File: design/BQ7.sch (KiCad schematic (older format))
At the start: 0 parts

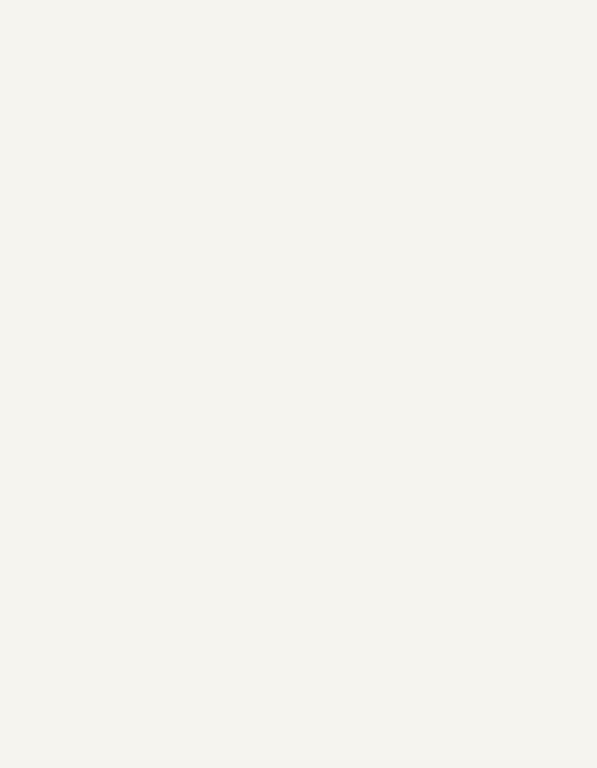
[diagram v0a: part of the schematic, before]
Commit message: Add new component bq and other libs also fix lib path. Project is now portable
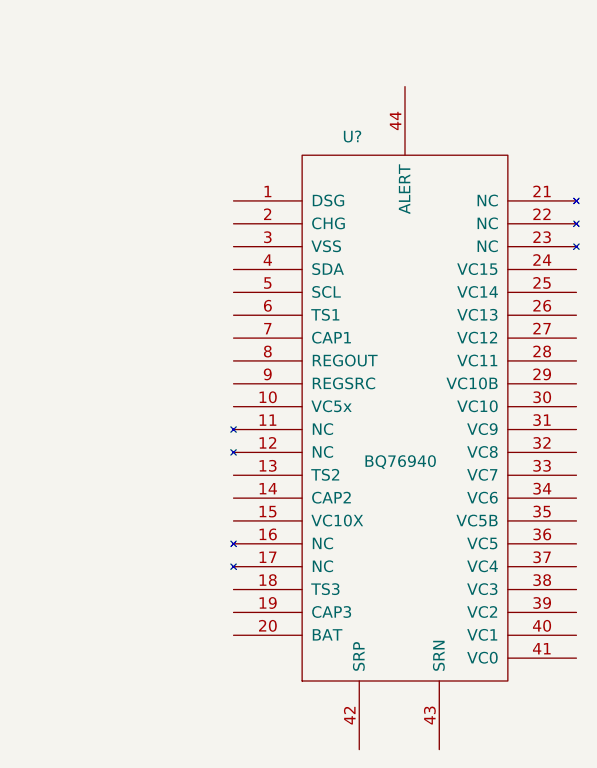
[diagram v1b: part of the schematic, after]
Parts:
- added U?: BQ76940, MODULE, symbol BQ76940
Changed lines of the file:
@@
 EESchema Schematic File Version 2
+LIBS:iso5500
+LIBS:crf_1
+LIBS:BQ76940
 LIBS:power
 LIBS:device
@@
 LIBS:contrib
 LIBS:valves
+LIBS:BMS-cache
 EELAYER 25 0
 EELAYER END
@@
 Text Notes 1150 1050 0    60   ~ 0
 Bq7*** circuit its basicly disconnetced from other stuff looking a\n voltage of every cell and if needed discharging them.(balancing)\nControled by a MCU two of them because we have 30 batterys.
+$Comp
+L BQ76940 U?
+U 1 1 55BBBEDC
+P 8550 2500
+F 0 "U?" H 8320 3730 50  0000 C CNN
+F 1 "BQ76940" H 8530 2310 50  0000 C CNN
+F 2 "MODULE" H 8590 3300 50  0001 C CNN
+F 3 "DOCUMENTATION" H 8500 930 50  0001 C CNN
+	1    8550 2500
+	1    0    0    -1
+$EndComp
 $EndSCHEMATC

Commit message: Some modification and started job
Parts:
- removed U?: BQ76940, MODULE, symbol BQ76940
- added C? (x3): 0.1u, symbol C
- added C?: 4.7u, symbol C
- added C? (x4): Cf, symbol C
- added C? (x2): C, symbol C
- added D? (x3): DIODE, symbol DIODE
- added D? (x2): DIODESCH, symbol DIODESCH
- added Q?: MOSFET_N, symbol MOSFET_N
- added R?: 1M, symbol R
- added R? (x3): 50k, symbol R
- added R?: SHUNT, symbol SHUNT
- added R? (x2): 100, symbol R
- added R?: Rgate, symbol R
- added R?: Rdrain, symbol R
- added R?: Rf 1M, symbol R
- added R?: Rd, symbol R
- added R?: Rsrc, symbol R
- added U?: BQ76940, MODULE, symbol BQ76940
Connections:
- new net: R?.1, U?.44 (ALERT)
- new net: R?.2, R?.3
- new net: R?.2, R?.4
- new net: C?.1, C?.1, R?.1, U?.43 (SRN)
- new net: C?.1, C?.2, R?.1
- new net: C?.1, U?.7 (CAP1)
- new net: C?.2, R?.2, U?.9 (REGSRC)
- new net: D?.2 (K), Q?.G, R?.1
- new net: D?.2 (K), Q?.D, R?.1
- new net: D?.1 (A), D?.1 (A), D?.2 (K), Q?.S, R?.1
- new net: D?.1 (A), D?.1 (A)
- new net: D?.2 (K), R?.1, R?.2
- new net +BATT: R?.2, R?.2
- new net -BATT: R?.1
- new net BATT: C?.1, C?.2, D?.2 (K), R?.1, U?.20 (BAT)
- new net GND: C?.1, C?.1, C?.2, C?.2, C?.2, C?.2, R?.1, R?.1, R?.1, R?.2, R?.2, U?.3 (VSS)
- new net NTC Temp monitor/Temp1_in: R?.2, U?.6 (TS1)
- new net NTC Temp monitor/Temp2_in: R?.2, U?.13 (TS2)
- new net NTC Temp monitor/Temp3_in: R?.2, U?.18 (TS3)
- new net SCL: U?.5 (SCL)
- new net SDA: U?.4 (SDA)
- new net VC10X: C?.1, C?.2, C?.2, R?.2, U?.15 (VC10X)
- new net VC15: D?.1 (A)
- new net VC5X: C?.1, C?.2, U?.10 (VC5x)
- new net Vcc: C?.1, U?.8 (REGOUT)
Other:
- note added: "Capactior between termistors"
- note added: "Dont forget this when programming"
- note added: "Max BAT-VSS = 36V/25V\nso R must be quite high \n1M"
- note added: "Pin configuration\n"
- note added: "Should be high value\n"

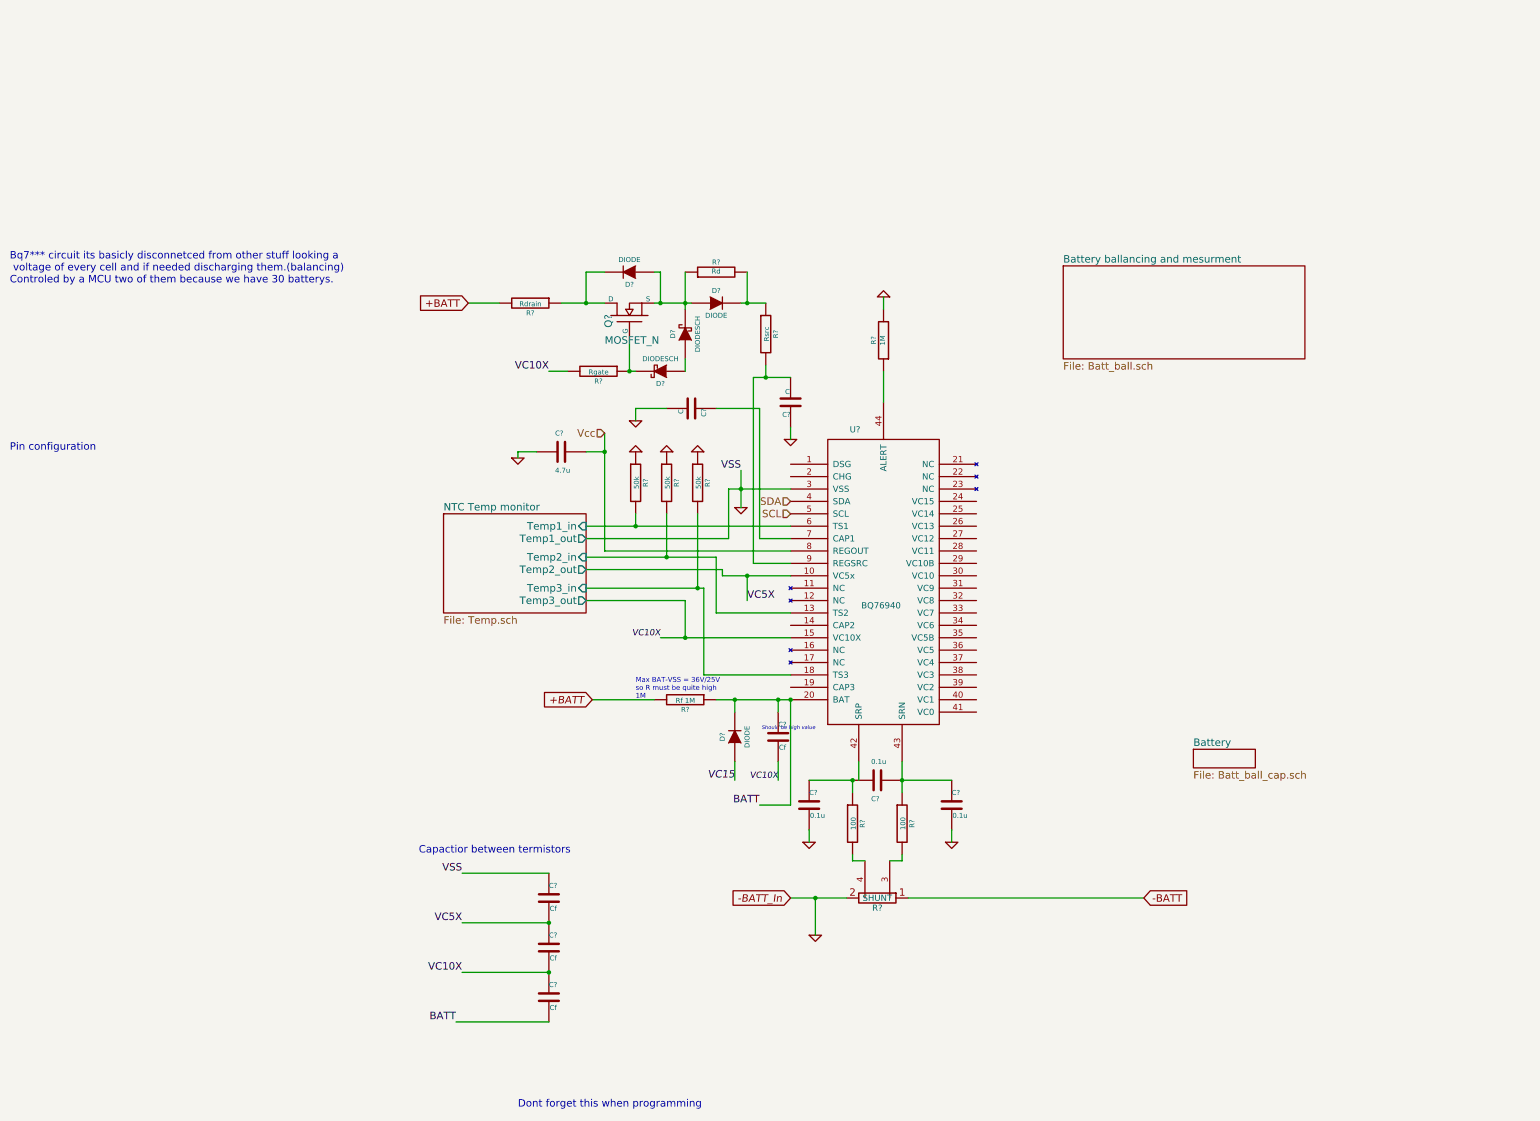
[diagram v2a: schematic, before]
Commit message: Add a cell to 10 but currently a scheme is a total mess fix it
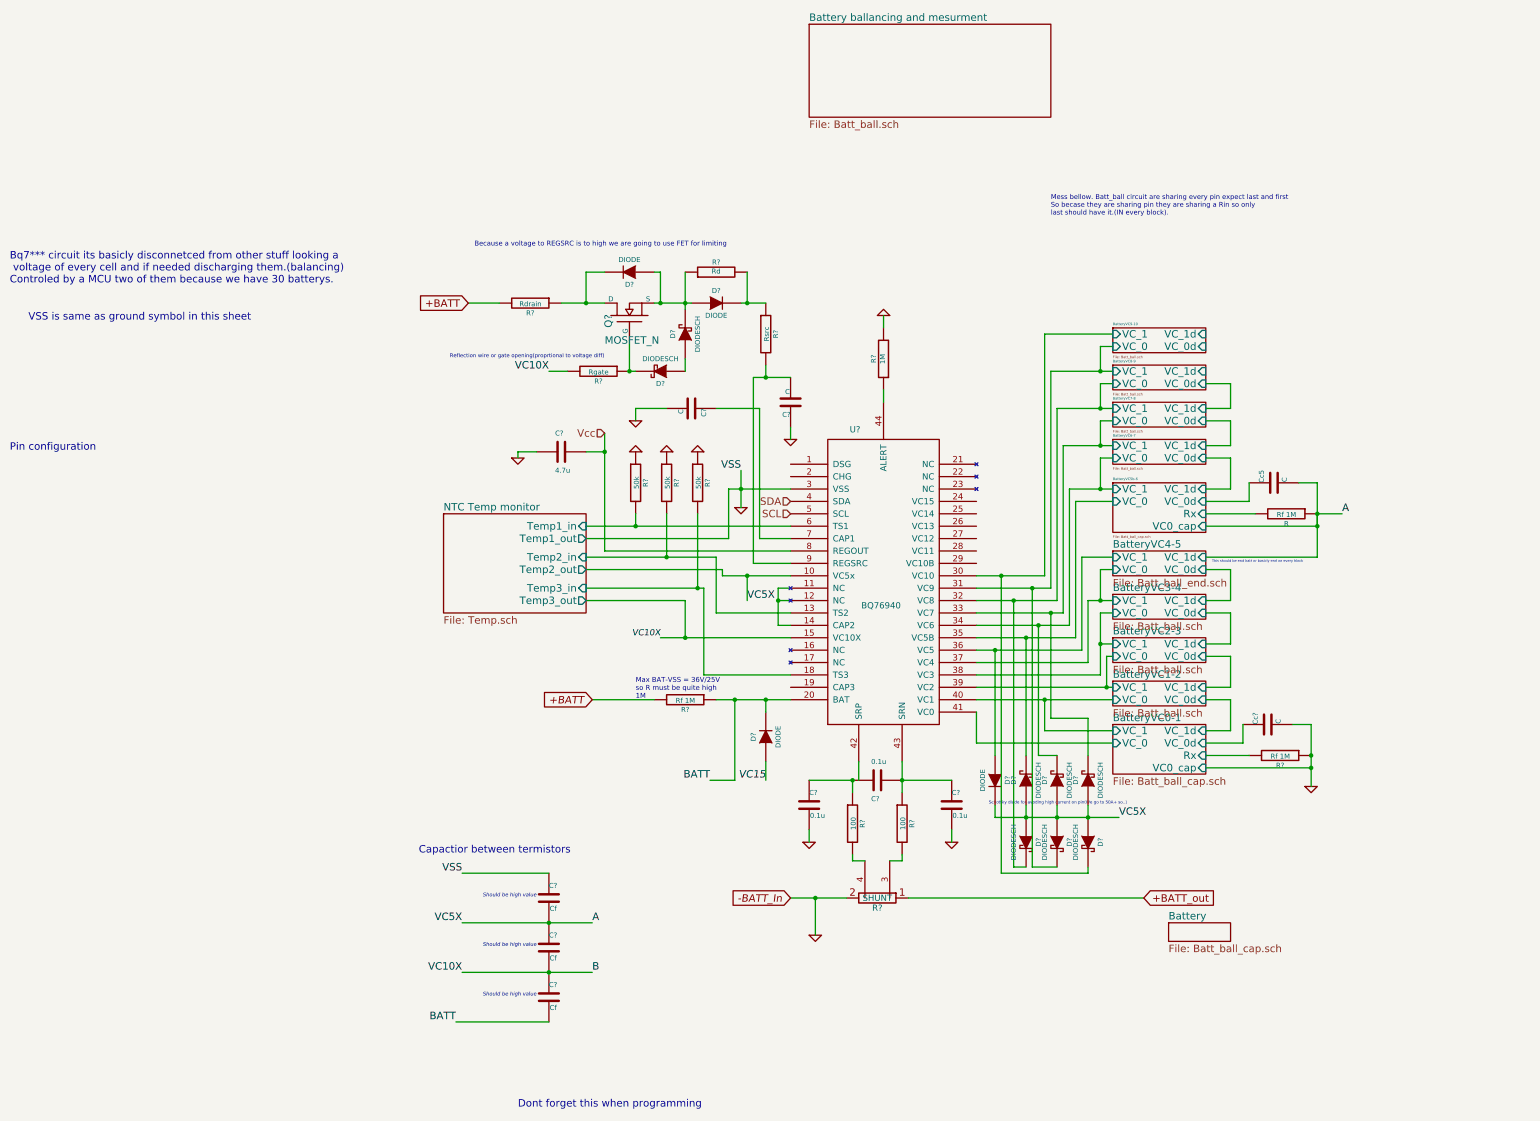
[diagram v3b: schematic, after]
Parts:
- removed C?: Cf, symbol C
- added Cc5, Cc?: C, symbol C
- added D?: DIODE, symbol DIODE
- added D? (x6): DIODESCH, symbol DIODESCH
- added R, R?: Rf 1M, symbol R
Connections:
- net GND: now also Cc?.2, R?.1
- net at U?.11 (NC): now also U?.12 (NC), U?.14 (CAP2)
- net BatteryVC9-10/VC_1: now reaches U?.30 (VC10)
- net BatteryVC9-10/VC_1: now also D?.2 (K)
- net BatteryVC8-9/VC_1: now reaches U?.31 (VC9)
- net BatteryVC8-9/VC_1: now also D?.2 (K)
- net BatteryVC7-8/VC_1: now reaches U?.32 (VC8)
- net BatteryVC7-8/VC_1: now also D?.2 (K)
- net BatteryVC6-7/VC_1: now reaches U?.33 (VC7)
- net BatteryVC6-7/VC_1: now also D?.2 (K)
- net BatteryVC5b-6/VC_1: now reaches U?.34 (VC6)
- net BatteryVC5b-6/VC_1: now also D?.2 (K)
- net BatteryVC5b-6/VC_0: now reaches U?.35 (VC5B)
- net BatteryVC5b-6/VC_0: now also D?.2 (K)
- net BatteryVC4-5/VC_1: now reaches U?.36 (VC5)
- net BatteryVC4-5/VC_1: now also D?.1 (A)
- net BatteryVC3-4/VC_1: now reaches U?.37 (VC4)
- net BatteryVC2-3/VC_1: now reaches U?.38 (VC3)
- net BatteryVC1-2/VC_1: now reaches U?.39 (VC2)
- net BatteryVC0-1/VC_1: now reaches U?.40 (VC1)
- net BatteryVC0-1/VC_0: now reaches U?.41 (VC0)
- net -BATT renamed +BATT_out
- net VC10X renamed B
- net VC5X renamed A
- net A: now also Cc5.2, D?.1 (A), D?.1 (A), D?.1 (A), D?.1 (A), D?.1 (A), D?.1 (A), D?.2 (K), R.1
- new net BatteryVC0-1/Rx: R?.2
- new net BatteryVC0-1/VC_0d: Cc?.1
- new net BatteryVC5b-6/Rx: R.2
- new net BatteryVC5b-6/VC_0d: Cc5.1
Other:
- note added: "Because a voltage to REGSRC is to high we are going to use FET for limiting"
- note added: "Mess bellow. Batt_ball circuit are sharing every pin expect last and first\nSo becase they are sharing pin they are sharing a Rin so only\nlast should have it.(IN every block)."
- note added: "Reflection wire or gate opening(proprtional to voltage diff)"
- note added: "Schottky diode for avoding high current on pin(We go to 50A+ so..)"
- note added: "This should be end batt or basicly end on every block"
- note added: "VSS is same as ground symbol in this sheet"
- moved on the sheet: D?, R?

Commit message: Fix BQ scheme so it's more readable
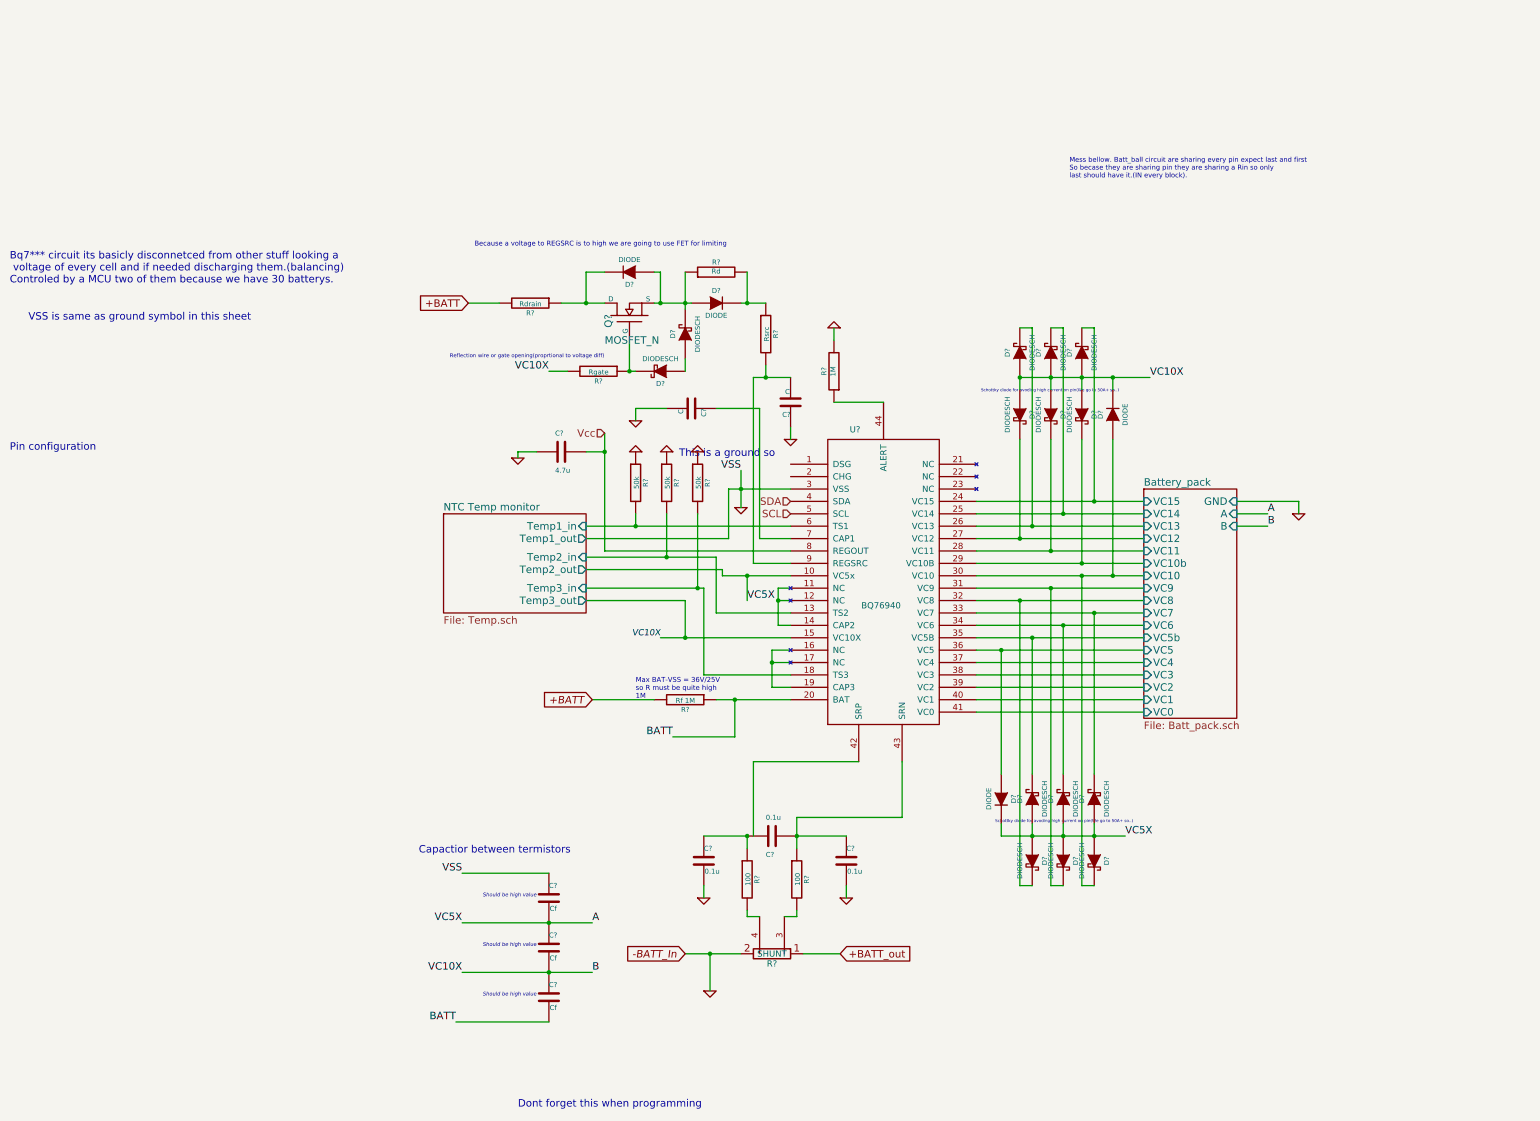
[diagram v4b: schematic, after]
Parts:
- removed Cc5, Cc?: C, symbol C
- removed D?: DIODE, symbol DIODE
- removed R, R?: Rf 1M, symbol R
- added D?: DIODE, symbol DIODE
- added D? (x6): DIODESCH, symbol DIODESCH
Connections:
- net B: now also D?.1 (A), D?.1 (A), D?.1 (A), D?.1 (A), D?.1 (A), D?.1 (A), D?.2 (K)
- net at U?.16 (NC): now also U?.17 (NC), U?.19 (CAP3)
- net Battery_pack/VC15: now reaches U?.24 (VC15)
- net Battery_pack/VC15: now also D?.2 (K)
- net Battery_pack/VC14: now reaches U?.25 (VC14)
- net Battery_pack/VC14: now also D?.2 (K)
- net Battery_pack/VC13: now reaches U?.26 (VC13)
- net Battery_pack/VC13: now also D?.2 (K)
- net Battery_pack/VC12: now reaches U?.27 (VC12)
- net Battery_pack/VC12: now also D?.2 (K)
- net Battery_pack/VC11: now reaches U?.28 (VC11)
- net Battery_pack/VC11: now also D?.2 (K)
- net Battery_pack/VC10b: now reaches U?.29 (VC10B)
- net Battery_pack/VC10b: now also D?.2 (K)
- net BatteryVC0-1/VC_0 renamed Battery_pack/VC0
- net BatteryVC0-1/VC_1 renamed Battery_pack/VC1
- net BatteryVC1-2/VC_1 renamed Battery_pack/VC2
- net BatteryVC2-3/VC_1 renamed Battery_pack/VC3
- net BatteryVC3-4/VC_1 renamed Battery_pack/VC4
- net BatteryVC4-5/VC_1 renamed Battery_pack/VC5
- net BatteryVC5b-6/VC_0 renamed Battery_pack/VC5b
- net BatteryVC5b-6/VC_1 renamed Battery_pack/VC6
- net BatteryVC6-7/VC_1 renamed Battery_pack/VC7
- net BatteryVC7-8/VC_1 renamed Battery_pack/VC8
- net BatteryVC8-9/VC_1 renamed Battery_pack/VC9
- net BatteryVC9-10/VC_1 renamed Battery_pack/VC10
- net Battery_pack/VC10: now also D?.1 (A)
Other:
- note added: "This is a ground so"
- note removed: "This should be end batt or basicly end on every block"
- moved on the sheet: C?, D?, R?
